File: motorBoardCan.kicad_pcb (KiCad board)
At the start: 6 copper layers, 50 x 50 mm, 45 parts, among them J1 Conn_01x04_Pin, J2 Conn_01x04_Pin, J3 Conn_02x04_Top_Bottom, J4 Conn_01x02_Socket, J5 Conn_01x02_Socket, J6 Conn_02x04_Top_Bottom, U1 NUCLEO-G431KB, U10 TPS563200, U2 LMD18200, U4 SN65HVD230, U5 LD1117S33TR_SOT223, U6 LMD18200

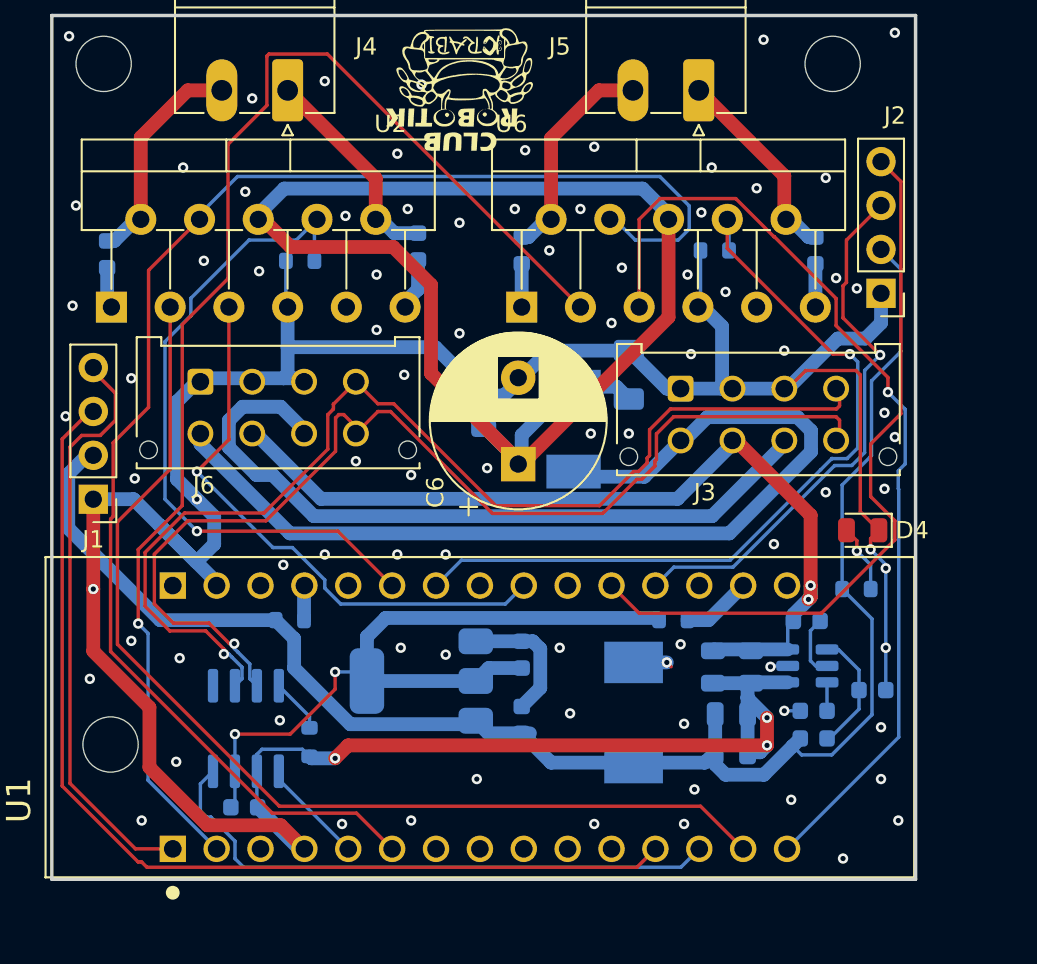
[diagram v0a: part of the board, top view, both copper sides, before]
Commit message: fix warning, separate brake commands, add JLCJLCJLC, enlarge capacitors, tune routing
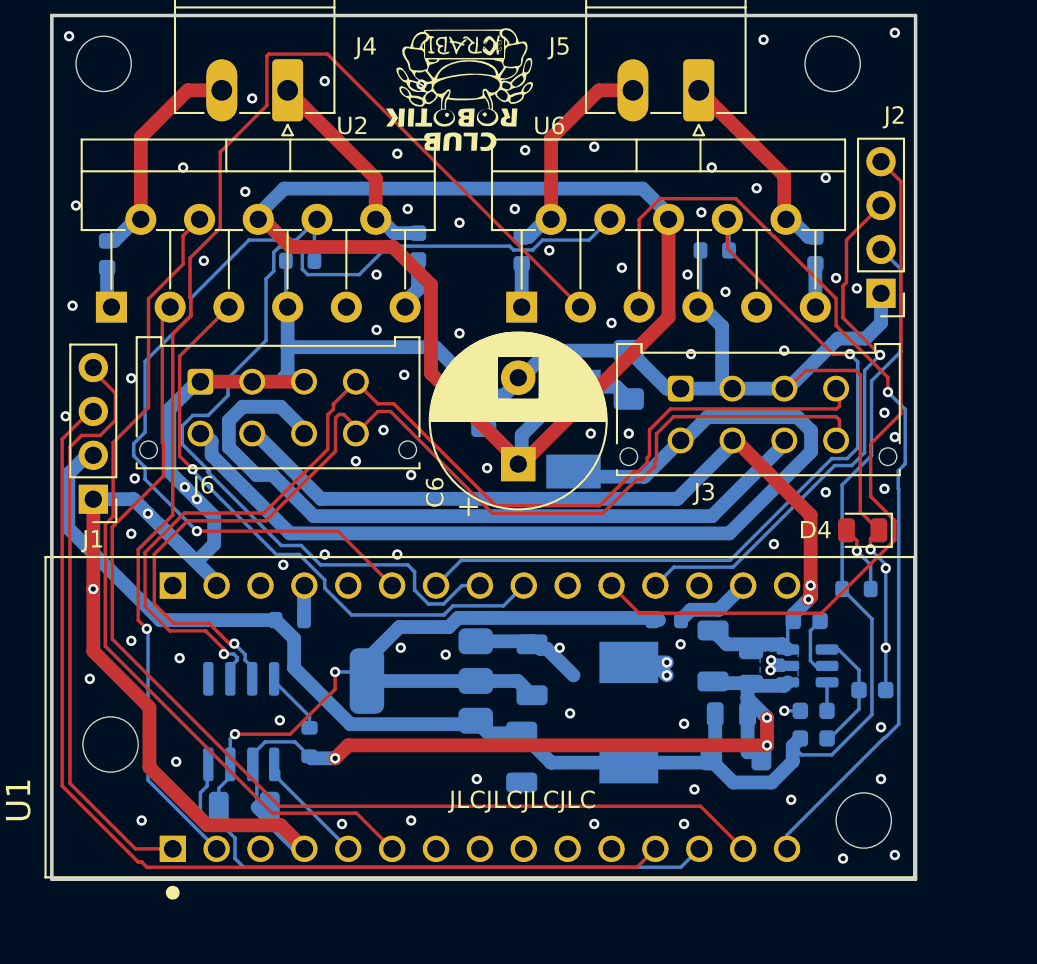
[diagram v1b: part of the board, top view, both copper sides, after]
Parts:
- added ?: , , F.Cu at (123.8, 104.0)
- C1, C2, C3: footprint Capacitor_SMD:C_0603_1608Metric -> Capacitor_SMD:C_1206_3216Metric
- C22, C25: footprint LED_SMD:LED_0805_2012Metric -> Capacitor_SMD:C_1206_3216Metric
- moved C2 2.15 mm to (104.0, 100.3), turned to -90 degrees
- moved C3 1.06 mm to (104.6, 95.3)
- moved C22 0.64 mm to (115.1, 94.5)
- moved U4 0.48 mm to (87.8, 98.3)
- moved R2 0.38 mm to (112.4, 92.4)
- moved C25 0.30 mm to (116.4, 100.2)
- moved L2 0.27 mm to (110.2, 97.8)
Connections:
- U1 pad 3_6: /BRAKE_A -> /BRAKE_B
- U1 pad 4_8: unconnected-(U1B-PA5-Pad4_8) -> /BRAKE_A
- U2 pad 4: /BRAKE_A -> /BRAKE_B
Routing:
- net /BRAKE_B: track 0.00 -> 48.4 mm
- net /BRAKE_A: track 85.0 -> 58.5 mm
- net /DCDC_5V/SW_DCDC5V: track 13.2 -> 25.5 mm, vias 3 -> 5
- net /PWM_B: track 33.1 -> 34.6 mm
- net /CURRENT_B: track 39.4 -> 40.9 mm
- net GND: track 197.0 -> 197.9 mm
- net 5V: track 94.4 -> 95.3 mm
- net CAN_R: track 33.9 -> 34.6 mm
- net CAN+: track 63.9 -> 63.3 mm
- added copper zone on B.Cu, net /DCDC_5V/SW_DCDC5V
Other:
- board text added: "JLCJLCJLCJLC"

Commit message: First Commit , BOM
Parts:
- removed ?: , 
- C21, C24: footprint LED_SMD:LED_0805_2012Metric -> Capacitor_SMD:C_0805_2012Metric
- C22, C25: footprint Capacitor_SMD:C_1206_3216Metric -> Capacitor_SMD:C_0805_2012Metric
- C7: value 10µF -> 10uF
- D1: footprint Diode_SMD:D_1206_3216Metric -> Capacitor_SMD:C_0805_2012Metric
- D4: value LED_Small -> LED_G
- R4: value 220R -> 2kR
- moved H4 42.2 mm to (123.8, 104.0)
- moved C7 0.21 mm to (101.7, 80.5)

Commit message: fix warnings (mainly silkscreen)
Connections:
- U1 pad 3_1: /ENC1_B -> /ENC1_A
- U1 pad 3_12: /ENC1_A -> /ENC1_B
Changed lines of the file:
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@@
 		)
 		(property ki_fp_filters "Connector*:*_2x??_*")
-		(sheetname "Root")
+		(sheetname "Racine")
 		(sheetfile "motorBoardCan.kicad_sch")
 		(attr through_hole)
@@
 		)
 		(property ki_fp_filters "MountingHole*")
-		(sheetname "Root")
+		(sheetname "Racine")
 		(sheetfile "motorBoardCan.kicad_sch")
 		(attr exclude_from_pos_files exclude_from_bom)
@@
 		)
 		(property ki_fp_filters "Connector*:*_1x??_*")
-		(sheetname "Root")
+		(sheetname "Racine")
 		(sheetfile "motorBoardCan.kicad_sch")
 		(attr through_hole)
@@
 		)
 		(property ki_fp_filters "CP_*")
-		(sheetname "Root")
+		(sheetname "Racine")
 		(sheetfile "motorBoardCan.kicad_sch")
 		(attr through_hole)
@@
 		)
 		(property ki_fp_filters "Connector*:*_2x??_*")
-		(sheetname "Root")
+		(sheetname "Racine")
 		(sheetfile "motorBoardCan.kicad_sch")
 		(attr through_hole)
@@
 		)
 		(property ki_fp_filters "MountingHole*")
-		(sheetname "Root")
+		(sheetname "Racine")
 		(sheetfile "motorBoardCan.kicad_sch")
 		(attr exclude_from_pos_files exclude_from_bom)
@@
 			(layer "Cmts.User")
 		)
-		(fp_circle
-			(center 0 0)
-			(end 3.45 0)
-			(stroke
-				(width 0.05)
-				(type solid)
-			)
-			(fill none)
-			(layer "F.CrtYd")
-		)
 		(fp_text user "${REFERENCE}"
 			(at 0 0 0)
@@
 		)
 		(property ki_fp_filters "Connector*:*_1x??_*")
-		(sheetname "Root")
+		(sheetname "Racine")
 		(sheetfile "motorBoardCan.kicad_sch")
 		(attr through_hole)
@@
 			)
 		)
-		(sheetname "Root")
+		(sheetname "Racine")
 		(sheetfile "motorBoardCan.kicad_sch")
 		(attr through_hole)
@@
 			(layers "*.Cu" "*.Mask")
 			(remove_unused_layers no)
-			(net 35 "/ENC1_B")
+			(net 36 "/ENC1_A")
 			(pinfunction "PA9")
 			(pintype "bidirectional")
@@
 			(layers "*.Cu" "*.Mask")
 			(remove_unused_layers no)
-			(net 36 "/ENC1_A")
+			(net 35 "/ENC1_B")
 			(pinfunction "PA8")
 			(pintype "bidirectional")
@@
 		)
 		(property ki_fp_filters "MountingHole*")
-		(sheetname "Root")
+		(sheetname "Racine")
 		(sheetfile "motorBoardCan.kicad_sch")
 		(attr exclude_from_pos_files exclude_from_bom)
@@
 		)
 		(property ki_fp_filters "MountingHole*")
-		(sheetname "Root")
+		(sheetname "Racine")
 		(sheetfile "motorBoardCan.kicad_sch")
 		(attr board_only exclude_from_pos_files exclude_from_bom)
@@
 			(layer "Cmts.User")
 		)
-		(fp_circle
-			(center 0 0)
-			(end 3.45 0)
-			(stroke
-				(width 0.05)
-				(type solid)
-			)
-			(fill none)
-			(layer "F.CrtYd")
-		)
 		(fp_text user "${REFERENCE}"
 			(at 0 0 0)
@@
 			)
 		)
+		(property "Availability" ""
+			(at 0 0 -90)
+			(unlocked yes)
+			(layer "B.Fab")
+			(hide yes)
+			(effects
+				(font
+					(size 1 1)
+					(thickness 0.15)
+				)
+				(justify mirror)
+			)
+		)
+		(property "Check_prices" ""
+			(at 0 0 -90)
+			(unlocked yes)
+			(layer "B.Fab")
+			(hide yes)
+			(effects
+				(font
+					(size 1 1)
+					(thickness 0.15)
+				)
+				(justify mirror)
+			)
+		)
+		(property "DESCRIPTION" ""
+			(at 0 0 -90)
+			(unlocked yes)
+			(layer "B.Fab")
+			(hide yes)
+			(effects
+				(font
+					(size 1 1)
+					(thickness 0.15)
+				)
+				(justify mirror)
+			)
+		)
+		(property "DIGI-KEY_PART_NUMBER" ""
+			(at 0 0 -90)
+			(unlocked yes)
+			(layer "B.Fab")
+			(hide yes)
+			(effects
+				(font
+					(size 1 1)
+					(thickness 0.15)
+				)
+				(justify mirror)
+			)
+		)
+		(property "Description_1" ""
+			(at 0 0 -90)
+			(unlocked yes)
+			(layer "B.Fab")
+			(hide yes)
+			(effects
+				(font
+					(size 1 1)
+					(thickness 0.15)
+				)
+				(justify mirror)
+			)
+		)
+		(property "MF" ""
+			(at 0 0 -90)
+			(unlocked yes)
+			(layer "B.Fab")
+			(hide yes)
+			(effects
+				(font
+					(size 1 1)
+					(thickness 0.15)
+				)
+				(justify mirror)
+			)
+		)
+		(property "MP" ""
+			(at 0 0 -90)
+			(unlocked yes)
+			(layer "B.Fab")
+			(hide yes)
+			(effects
+				(font
+					(size 1 1)
+					(thickness 0.15)
+				)
+				(justify mirror)
+			)
+		)
+		(property "PACKAGE" ""
+			(at 0 0 -90)
+			(unlocked yes)
+			(layer "B.Fab")
+			(hide yes)
+			(effects
+				(font
+					(size 1 1)
+					(thickness 0.15)
+				)
+				(justify mirror)
+			)
+		)
+		(property "PURCHASE-URL" ""
+			(at 0 0 -90)
+			(unlocked yes)
+			(layer "B.Fab")
+			(hide yes)
+			(effects
+				(font
+					(size 1 1)
+					(thickness 0.15)
+				)
+				(justify mirror)
+			)
+		)
+		(property "Package" ""
+			(at 0 0 -90)
+			(unlocked yes)
+			(layer "B.Fab")
+			(hide yes)
+			(effects
+				(font
+					(size 1 1)
+					(thickness 0.15)
+				)
+				(justify mirror)
+			)
+		)
+		(property "Price" ""
+			(at 0 0 -90)
+			(unlocked yes)
+			(layer "B.Fab")
+			(hide yes)
+			(effects
+				(font
+					(size 1 1)
+					(thickness 0.15)
+				)
+				(justify mirror)
+			)
+		)
+		(property "SnapEDA_Link" ""
+			(at 0 0 -90)
+			(unlocked yes)
+			(layer "B.Fab")
+			(hide yes)
+			(effects
+				(font
+					(size 1 1)
+					(thickness 0.15)
+				)
+				(justify mirror)
+			)
+		)
+		(property "LCSC#" "C845025"
+			(at 0 0 -90)
+			(unlocked yes)
+			(layer "B.Fab")
+			(hide yes)
+			(effects
+				(font
+					(size 1 1)
+					(thickness 0.15)
+				)
+				(justify mirror)
+			)
+		)
 		(sheetname "DCDC_5V")
 		(sheetfile "DCDC_5V.kicad_sch")
@@
 		(tags "capacitor")
 		(property "Reference" "C22"
-			(at 0 1.68 90)
+			(at -2.275 -0.125 180)
 			(layer "B.SilkS")
 			(effects
@@
 		)
 		(property ki_fp_filters "*Fuse*")
-		(sheetname "Root")
+		(sheetname "Racine")
 		(sheetfile "motorBoardCan.kicad_sch")
 		(attr smd)
@@
 		)
 		(property ki_fp_filters "C_*")
-		(sheetname "Root")
+		(sheetname "Racine")
 		(sheetfile "motorBoardCan.kicad_sch")
 		(attr smd)
@@
 		)
 		(property ki_fp_filters "C_*")
-		(sheetname "Root")
+		(sheetname "Racine")
 		(sheetfile "motorBoardCan.kicad_sch")
 		(attr smd)
@@
 		(tags "capacitor")
 		(property "Reference" "C21"
-			(at 0 1.68 90)
+			(at -2.2125 -0.425 180)
 			(layer "B.SilkS")
 			(effects
@@
 		)
 		(property ki_fp_filters "R_*")
-		(sheetname "Root")
+		(sheetname "Racine")
 		(sheetfile "motorBoardCan.kicad_sch")
 		(attr smd)
@@
 		)
 		(property ki_fp_filters "SOT?223*TabPin2*")
-		(sheetname "Root")
+		(sheetname "Racine")
 		(sheetfile "motorBoardCan.kicad_sch")
 		(attr smd)
@@
 		)
 		(property ki_fp_filters "C_*")
-		(sheetname "Root")
+		(sheetname "Racine")
 		(sheetfile "motorBoardCan.kicad_sch")
 		(attr smd)
@@
 		)
 		(property ki_fp_filters "R_*")
-		(sheetname "Root")
+		(sheetname "Racine")
 		(sheetfile "motorBoardCan.kicad_sch")
 		(attr smd)
@@
 		)
 		(property ki_fp_filters "TO-???* *_Diode_* *SingleDiode* D_*")
-		(sheetname "Root")
+		(sheetname "Racine")
 		(sheetfile "motorBoardCan.kicad_sch")
 		(attr smd)
@@
 		)
 		(property ki_fp_filters "C_*")
-		(sheetname "Root")
+		(sheetname "Racine")
 		(sheetfile "motorBoardCan.kicad_sch")
 		(attr smd)
@@
 		)
 		(property ki_fp_filters "R_*")
-		(sheetname "Root")
+		(sheetname "Racine")
 		(sheetfile "motorBoardCan.kicad_sch")
 		(attr smd)
@@
 		(tags "capacitor")
 		(property "Reference" "C24"
-			(at 0 1.68 180)
+			(at 0.3625 4.15 180)
 			(layer "B.SilkS")
 			(effects
@@
 		(tags "capacitor")
 		(property "Reference" "C25"
-			(at 0 1.68 180)
+			(at 0 3.3 180)
 			(layer "B.SilkS")
 			(effects
@@
 		)
 		(property ki_fp_filters "SOIC*3.9x4.9mm*P1.27mm*")
-		(sheetname "Root")
+		(sheetname "Racine")
 		(sheetfile "motorBoardCan.kicad_sch")
 		(attr smd)
@@
 		)
 		(height 4)
-		(gr_text "50.0000 mm"
+		(gr_text "50,0000 mm"
 			(at 101.8 110.3 0)
 			(layer "Dwgs.User")
@@
 		)
 		(height 4.6)
-		(gr_text "50.0000 mm"
+		(gr_text "50,0000 mm"
 			(at 71.1 82.4 90)
 			(layer "Dwgs.User")

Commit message: fine tuning
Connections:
- U1 pad 3_1: /ENC1_A -> /ENC1_B
- U1 pad 3_12: /ENC1_B -> /ENC1_A
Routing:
- net GND: vias 86 -> 88
